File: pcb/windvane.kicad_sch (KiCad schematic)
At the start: 0 parts

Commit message: schematic done, next up - layout
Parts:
- added C1, C2: 22u, Capacitor_SMD:C_Elec_5x5.8, symbol Device:C_Polarized_Small
- added C3, C6, C7: 0.1u, Capacitor_SMD:C_0805_2012Metric, symbol Device:C
- added C4, C5: 22p, Capacitor_SMD:C_0805_2012Metric, symbol Device:C
- added H1, H2, H3, H4: MountingHole, MountingHole:MountingHole_2.2mm_M2, symbol Mechanical:MountingHole
- added J1: Screw_Terminal_01x04, TerminalBlock_Phoenix:TerminalBlock_Phoenix_MKDS-1,5-4-5.08_1x04_P5.08mm_Horizontal, symbol Connector:Screw_Terminal_01x04
- added J2: Conn_01x04_Pin, Connector_JST:JST_EH_S4B-EH_1x04_P2.50mm_Horizontal, symbol Connector:Conn_01x04_Pin
- added R1, R10, R2, R3, R4, R5, R6, R7, R8, R9: 10k, Resistor_SMD:R_0805_2012Metric, symbol Device:R
- added SS40AF1: ~, Package_TO_SOT_THT:TO-92L_Inline, symbol custom:SS40AF
- added U1: ESP-12F, RF_Module:ESP-12E, symbol RF_Module:ESP-12F
- added U2: MCP2515-xSO, Package_SO:SOIC-18W_7.5x11.6mm_P1.27mm, symbol Interface_CAN_LIN:MCP2515-xSO
- added U3: AS5600-ASOT, Package_SO:Infineon_PG-DSO-8-43, symbol Sensor_Magnetic:AS5600
- added U4: DS18B20, Package_TO_SOT_THT:TO-92_Inline, symbol Sensor_Temperature:DS18B20
- added U5: ~, symbol custom:MiniStepDownConverter
- added U6: TJA1050, Package_SO:SOIC-8_3.9x4.9mm_P1.27mm, symbol custom:TJA1050
- added Y1: 8MHz, Crystal:Crystal_HC49-4H_Vertical, symbol Device:Crystal
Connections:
- new net: C5.2, U2.7 (OSC2), Y1.1
- new net: C4.2, U2.8 (OSC1), Y1.2
- new net: R7.2, U1.17 (GPIO2)
- new net: U2.1 (TXCAN), U6.1 (TXD)
- new net: U2.2 (RXCAN), U6.4 (RXD)
- new net: C3.1, R1.2, U1.1 (~{RST})
- new net: R2.2, U1.3 (EN)
- new net: R10.2, U2.17 (~{RESET})
- new net: R8.1, U1.16 (GPIO15)
- new net +12V: C1.1, J1.4 (Pin_4), SS40AF1.1 (Vs), U5.1 (IN+)
- new net +3V3: C2.1, C6.2, C7.2, R1.1, R10.1, R2.1, R3.1, R4.1, R5.1, R6.1, R7.1, R9.1, U1.8 (VCC), U2.18 (VDD), U3.1 (VDD5V), U3.2 (VDD3V3), U4.3 (V_{DD}), U5.3 (OUT+), U6.3 (VCC)
- new net CAN_HI: J1.2 (Pin_2), U6.7 (CANH)
- new net CAN_LOW: J1.1 (Pin_1), U6.6 (CANL)
- new net CAN_~{Int}: U1.4 (GPIO16), U2.12 (~{INT})
- new net GND: C1.2, C2.2, C3.2, C4.1, C5.1, C6.1, C7.1, J1.3 (Pin_3), J2.4 (Pin_4), R8.2, SS40AF1.3 (GND), U1.15 (GND), U2.9 (VSS), U3.4 (GND), U3.8 (DIR), U4.1 (GND), U5.2 (GND), U5.4 (GND), U6.2 (GND), U6.8 (S)
- new net MISO: U1.10 (MISO), U2.15 (SO)
- new net MOSI: U1.13 (MOSI), U2.14 (SI)
- new net SCL: R5.2, U1.20 (GPIO5), U3.7 (SCL)
- new net SCLK: U1.14 (SCLK), U2.13 (SCK)
- new net SDA: R4.2, U1.19 (GPIO4), U3.6 (SDA)
- new net Speed_Out: SS40AF1.2 (Out), U1.5 (GPIO14)
- new net Temp_DQ: R3.2, R9.2, U1.6 (GPIO12), U4.2 (DQ)
- new net uC_PRG: J2.1 (Pin_1), R6.2, U1.18 (GPIO0)
- new net uC_RXD: J2.3 (Pin_3), U1.21 (GPIO3/RXD)
- new net uC_TXD: J2.2 (Pin_2), U1.22 (GPIO1/TXD)
- new net ~{CS}: U1.12 (GPIO10), U2.16 (~{CS})
- no-connect marks 0 -> 13
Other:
- note added: "CAN/NMEA200 interface"
- note added: "Controller"
- note added: "Direction sensor"
- note added: "Input/Output"
- note added: "Power supply"
- note added: "Speed sensor"
- note added: "Temperature sensor"

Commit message: place & route
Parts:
- removed C1, C2: 22u, Capacitor_SMD:C_Elec_5x5.8, symbol Device:C_Polarized_Small
- removed C3: 0.1u, Capacitor_SMD:C_0805_2012Metric, symbol Device:C
- removed H1, H2: MountingHole, MountingHole:MountingHole_2.2mm_M2, symbol Mechanical:MountingHole
- removed J1: Screw_Terminal_01x04, TerminalBlock_Phoenix:TerminalBlock_Phoenix_MKDS-1,5-4-5.08_1x04_P5.08mm_Horizontal, symbol Connector:Screw_Terminal_01x04
- removed J2: Conn_01x04_Pin, Connector_JST:JST_EH_S4B-EH_1x04_P2.50mm_Horizontal, symbol Connector:Conn_01x04_Pin
- removed R3: 10k, Resistor_SMD:R_0805_2012Metric, symbol Device:R
- added C1, C2, C8: 10u, Capacitor_SMD:C_0805_2012Metric, symbol Device:C
- added J3: Conn_01x08_Socket, Connector_FFC-FPC:Molex_200528-0080_1x08-1MP_P1.00mm_Horizontal, symbol Connector:Conn_01x08_Socket
- added R11: 10k, Resistor_SMD:R_0805_2012Metric, symbol Device:R
- C6, C7: value 0.1u -> 10u
- U3: footprint Package_SO:Infineon_PG-DSO-8-43 -> Package_SO:SOIC-8_3.9x4.9mm_P1.27mm
- U5: footprint (none) -> Custom:MiniStepDownConverter
- U7: renamed from SS40AF1; value ~ -> SS40AF1
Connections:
- net +12V: now also C1.2, J3.8 (Pin_8)
- net +3V3: now also C2.2, C8.2, R11.1
- net CAN_HI: now also J3.6 (Pin_6)
- net CAN_LOW: now also J3.5 (Pin_5)
- net GND: now also C1.1, C2.1, C8.1, J3.1 (Pin_1)
- net Speed_Out: now also R11.2
- net uC_PRG: now also J3.4 (Pin_4)
- net uC_RXD: now also J3.2 (Pin_2)
- net uC_TXD: now also J3.3 (Pin_3)
- no-connect marks 13 -> 14
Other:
- moved on the sheet: U3, U4, U5, U7

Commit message: routing - done, next up - review
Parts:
- added JP1: SolderJumper_2_Bridged, Jumper:SolderJumper-2_P1.3mm_Bridged2Bar_Pad1.0x1.5mm, symbol Jumper:SolderJumper_2_Bridged
- added R3: 120, Resistor_SMD:R_0805_2012Metric, symbol Device:R
- J3: footprint Connector_FFC-FPC:Molex_200528-0080_1x08-1MP_P1.00mm_Horizontal -> Custom:CON_532610871
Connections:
- net +3V3: now also JP1.2 (B); no longer U5.3 (OUT+)
- net uC_RXD: now also J3.3 (Pin_3); no longer J3.2 (Pin_2)
- net uC_TXD: now also J3.2 (Pin_2); no longer J3.3 (Pin_3)
- net CAN_HI renamed CAN_+
- net CAN_+: now also J3.5 (Pin_5), R3.1; no longer J3.6 (Pin_6)
- net CAN_LOW renamed CAN_-
- net CAN_-: now also J3.6 (Pin_6), R3.2; no longer J3.5 (Pin_5)
- new net: JP1.1 (A), U5.3 (OUT+)

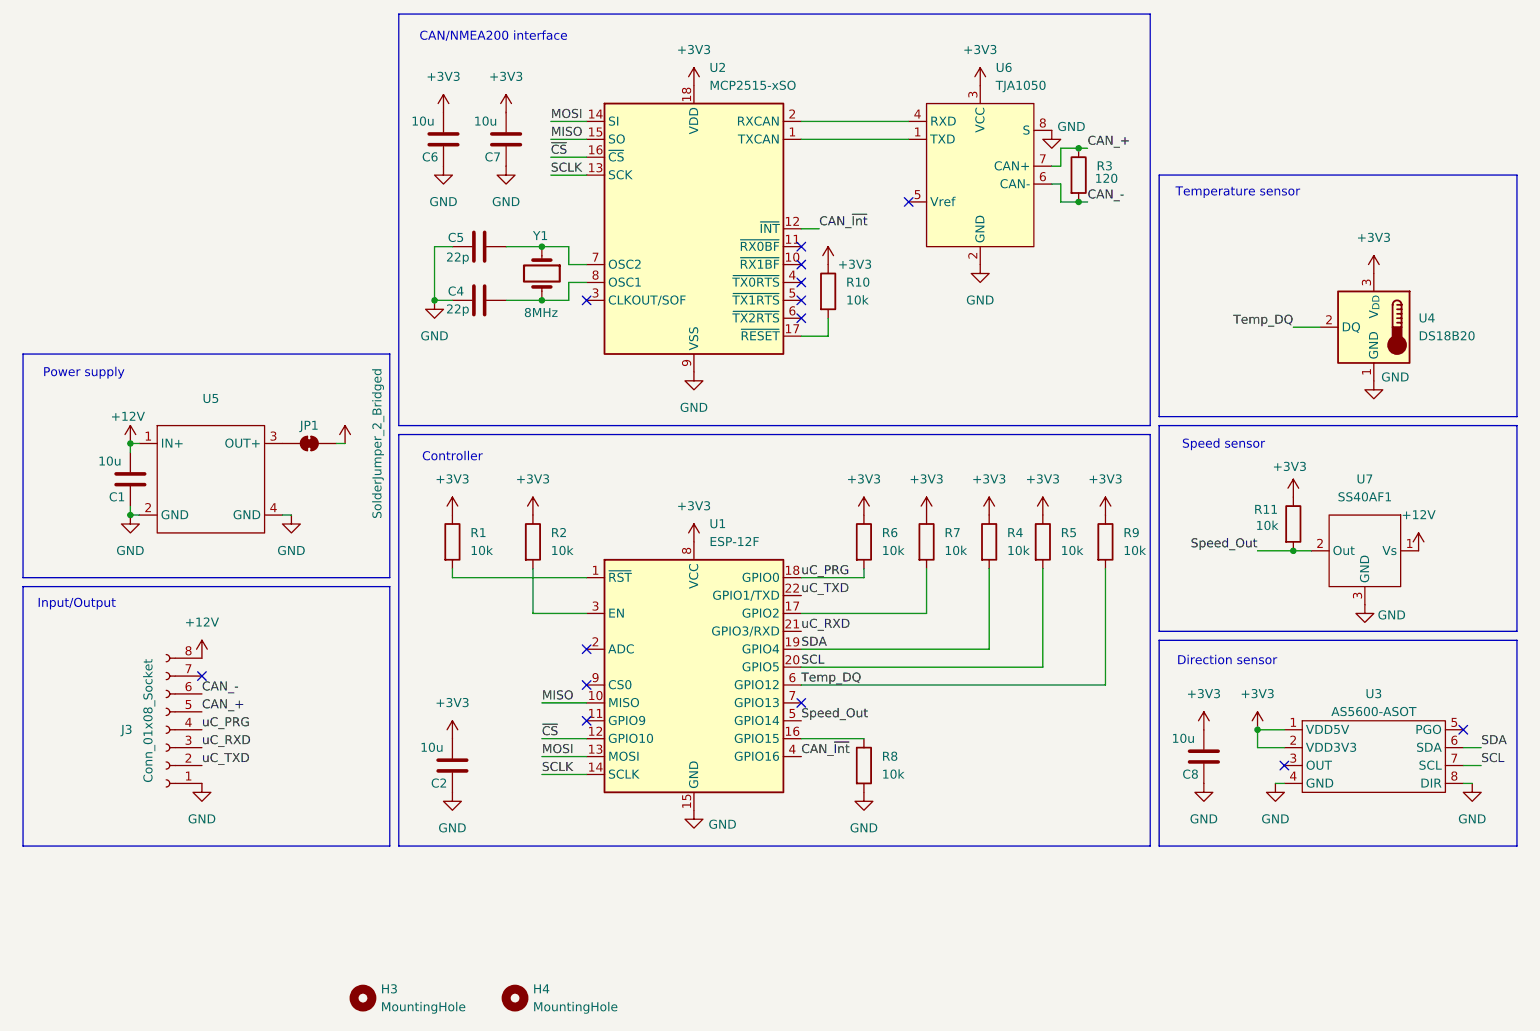
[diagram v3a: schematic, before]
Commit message: bugfixing: connected esp reset to connector, corrected wrong pin assigment of RPM sensor, improved routing, remapped CAN interrupt to GPIO9
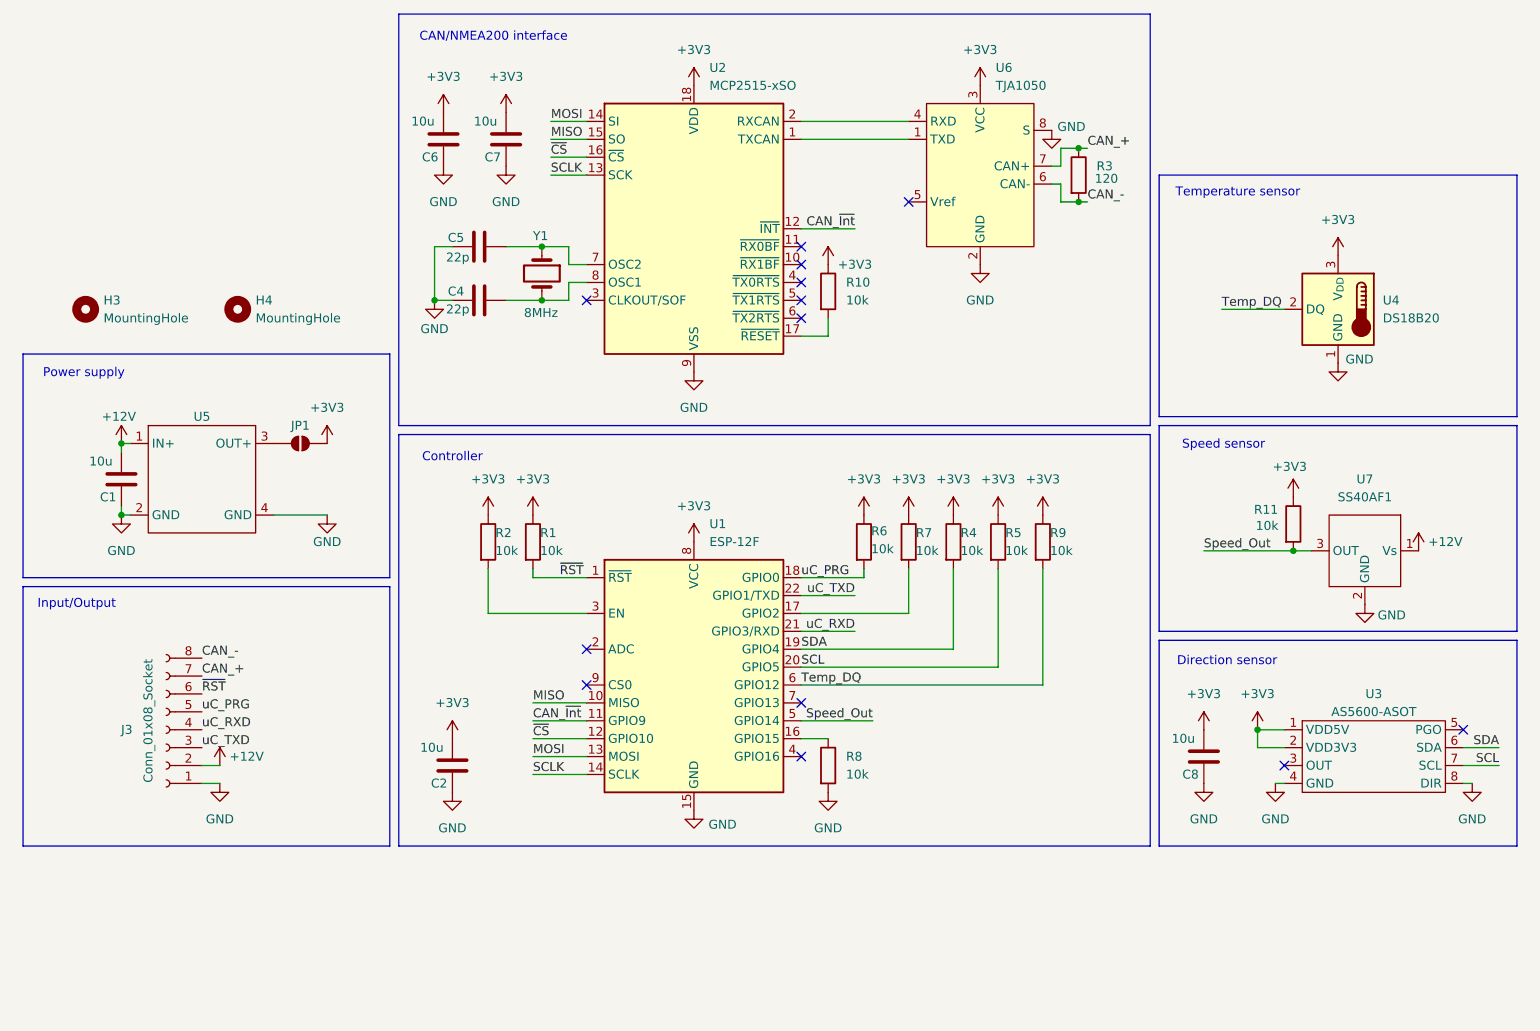
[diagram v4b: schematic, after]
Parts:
- removed JP1: SolderJumper_2_Bridged, Jumper:SolderJumper-2_P1.3mm_Bridged2Bar_Pad1.0x1.5mm, symbol Jumper:SolderJumper_2_Bridged
- added JP1: SolderJumper_2_Open, Jumper:SolderJumper-2_P1.3mm_Open_Pad1.0x1.5mm, symbol Jumper:SolderJumper_2_Open
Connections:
- net +12V: now also J3.2 (Pin_2); no longer J3.8 (Pin_8)
- net +3V3: now also JP1.2 (B)
- net CAN_+: now also J3.7 (Pin_7); no longer J3.5 (Pin_5)
- net CAN_-: now also J3.8 (Pin_8); no longer J3.6 (Pin_6)
- net CAN_~{Int}: now also U1.11 (GPIO9); no longer U1.4 (GPIO16)
- net GND: now also U7.2 (GND); no longer U7.3 (GND)
- net Speed_Out: now also U7.3 (OUT); no longer U7.2 (Out)
- net uC_PRG: now also J3.5 (Pin_5); no longer J3.4 (Pin_4)
- net uC_RXD: now also J3.4 (Pin_4); no longer J3.3 (Pin_3)
- net uC_TXD: now also J3.3 (Pin_3); no longer J3.2 (Pin_2)
- net ~{RST}: now reaches R1.2, U1.1 (~{RST})
- net ~{RST}: now also J3.6 (Pin_6)
- net at U5.3 (OUT+): now also JP1.1 (A)
- no-connect marks 14 -> 13
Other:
- moved on the sheet: C1, H3, H4, R1, R2, R4, R5, R7, R8, R9, U4, U5
